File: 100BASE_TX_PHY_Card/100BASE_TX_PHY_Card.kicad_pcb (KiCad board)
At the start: 2 copper layers, 54 parts, among them J1 Conn_02x11_Odd_Even, J2 RJ45_Amphenol_RJMG1BD3B8K1ANR, SW1 SW_DIP_x07, U1 LAN8710A, Y1 25M

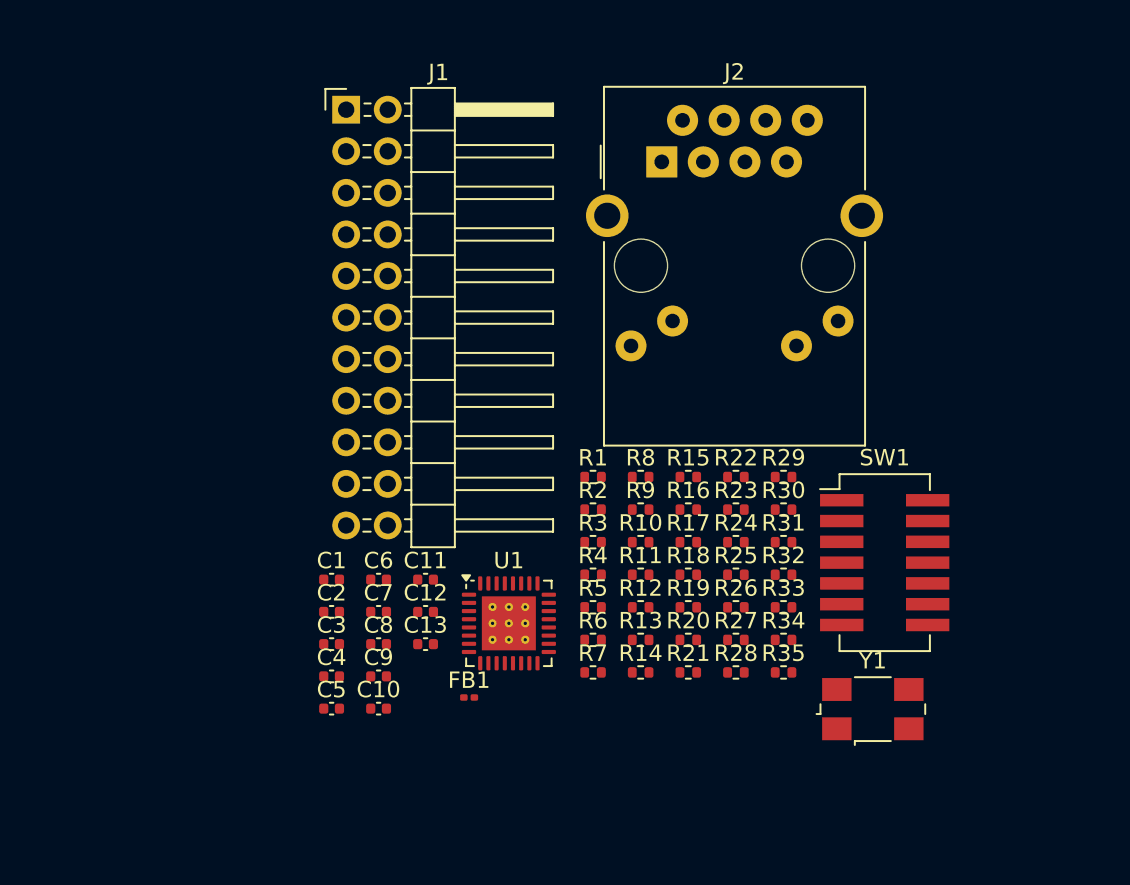
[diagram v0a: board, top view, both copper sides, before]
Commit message: LAN8710A PHY Card 4layer design
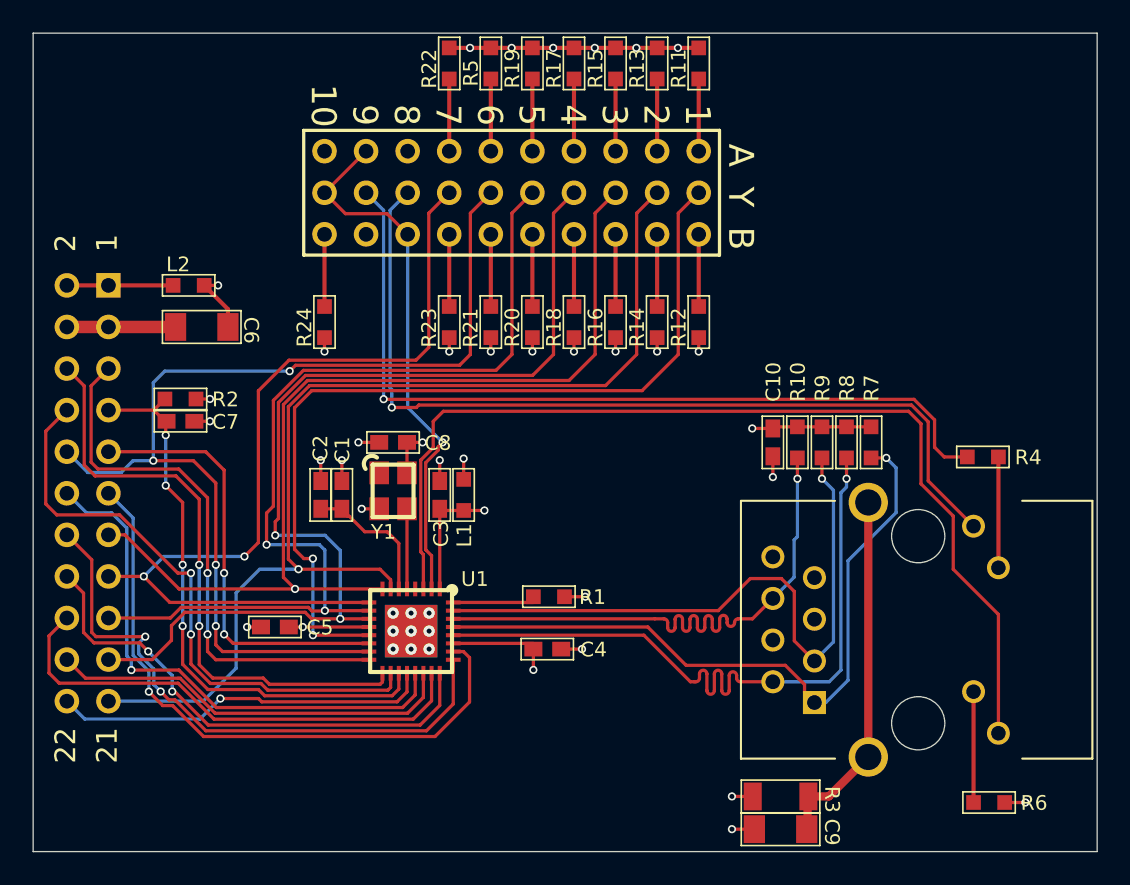
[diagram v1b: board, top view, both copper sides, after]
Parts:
- removed C11, C12, C13: dnp, Capacitor_SMD:C_0402_1005Metric
- removed FB1: FerriteBead, Resistor_SMD:R_0201_0603Metric
- removed J1: Conn_02x11_Odd_Even, Connector_PinHeader_2.54mm:PinHeader_2x11_P2.54mm_Horizontal
- removed J2: RJ45_Amphenol_RJMG1BD3B8K1ANR, Connector_RJ:RJ45_Amphenol_RJMG1BD3B8K1ANR
- removed R25, R26, R27, R28: 49,9, Resistor_SMD:R_0402_1005Metric
- removed R29: 0, Resistor_SMD:R_0402_1005Metric
- removed R30: 2,49k, Resistor_SMD:R_0402_1005Metric
- removed R31: 12.1k, Resistor_SMD:R_0402_1005Metric
- removed R32, R33: R, Resistor_SMD:R_0402_1005Metric
- removed R34, R35: 330, Resistor_SMD:R_0402_1005Metric
- removed SW1: SW_DIP_x07, Button_Switch_SMD:SW_DIP_SPSTx07_Slide_KingTek_DSHP07TJ_W5.25mm_P1.27mm_JPin
- added L1: Ferrite bead 120R/100MHz, pcSwitchLib.PcbLib:0603_IND, F.Cu at (142.3, 108.2)
- added L2: Ferrite bead 120R/100MHz, pcSwitchLib.PcbLib:0603_IND, F.Cu at (125.5, 95.4)
- added P1: RJMG1BD3B8K1ANR, pcSwitchLib.PcbLib:RJMG1BD3B8K1ANR, F.Cu at (170.1, 116.4)
- added P2: SELECTOR 10WAY, pcSwitchLib.PcbLib:SELECTOR_10WAY, F.Cu at (145.2, 89.8)
- added P3: Header 11X2H, Miscellaneous Connectors.IntLib:HDR2X11H, B.Cu at (120.6, 95.4)
- C1: value 30p -> 470pF 0603; footprint Capacitor_SMD:C_0402_1005Metric -> pcSwitchLib.PcbLib:0603_CAP
- C10: value dnp -> 15pF 0603; footprint Capacitor_SMD:C_0402_1005Metric -> pcSwitchLib.PcbLib:0603_CAP
- C2: value 30p -> 1uF 0603; footprint Capacitor_SMD:C_0402_1005Metric -> pcSwitchLib.PcbLib:0603_CAP
- C3, C4, C5: value 100n -> 100nF 0603; footprint Capacitor_SMD:C_0402_1005Metric -> pcSwitchLib.PcbLib:0603_CAP
- C6: value 4,7u -> 10uF 1206; footprint Capacitor_SMD:C_0402_1005Metric -> pcSwitchLib.PcbLib:1206_CAP
- C7: value 470p -> 100nF 0603; footprint Capacitor_SMD:C_0402_1005Metric -> pcSwitchLib.PcbLib:0603_CAP
- C8: value 1u -> 100nF 0603; footprint Capacitor_SMD:C_0402_1005Metric -> pcSwitchLib.PcbLib:0603_CAP
- C9: value dnp -> 10nF; footprint Capacitor_SMD:C_0402_1005Metric -> pcSwitchLib.PcbLib:1206_CAP
- R1: value 22 -> 12k1 0603; footprint Resistor_SMD:R_0402_1005Metric -> pcSwitchLib.PcbLib:0603
- R10, R9: value 1k -> 49R9 0603; footprint Resistor_SMD:R_0402_1005Metric -> pcSwitchLib.PcbLib:0603
- R11, R12, R13, R14, R15: value 1k -> 10k 0603; footprint Resistor_SMD:R_0402_1005Metric -> pcSwitchLib.PcbLib:0603
- R16, R17, R18, R19, R20, R21, R22: value 10k -> 10k 0603; footprint Resistor_SMD:R_0402_1005Metric -> pcSwitchLib.PcbLib:0603
- R2: value 22 -> 100k 0603; footprint Resistor_SMD:R_0402_1005Metric -> pcSwitchLib.PcbLib:0603
- R23: value 1M -> 10k 0603; footprint Resistor_SMD:R_0402_1005Metric -> pcSwitchLib.PcbLib:0603
- R24: value 2,49k -> 10k 0603; footprint Resistor_SMD:R_0402_1005Metric -> pcSwitchLib.PcbLib:0603
- R3: value 22 -> 1M 1206; footprint Resistor_SMD:R_0402_1005Metric -> pcSwitchLib.PcbLib:1206
- R4, R6: value 22 -> 330R 0603; footprint Resistor_SMD:R_0402_1005Metric -> pcSwitchLib.PcbLib:0603
- R5: value 22 -> 10k 0603; footprint Resistor_SMD:R_0402_1005Metric -> pcSwitchLib.PcbLib:0603
- R7, R8: value 22 -> 49R9 0603; footprint Resistor_SMD:R_0402_1005Metric -> pcSwitchLib.PcbLib:0603
- U1: footprint Package_DFN_QFN:QFN-32-1EP_5x5mm_P0.5mm_EP3.3x3.3mm_ThermalVias -> pcSwitchLib.PcbLib:LAN8710A
- Y1: value 25M -> 25MHz 3225; footprint Crystal:Crystal_SMD_0603-4Pin_6.0x3.5mm -> pcSwitchLib.PcbLib:XTAL_3225
- moved R13 35.2 mm to (154.1, 81.9), turned to -90 degrees
- moved R19 34.6 mm to (146.5, 81.9), turned to -90 degrees
- moved R5 33.8 mm to (144.0, 81.9), turned to -90 degrees
- moved Y1 32.2 mm to (138.0, 108.0), turned to -90 degrees
- moved R11 31.4 mm to (156.7, 81.9), turned to -90 degrees
- moved R22 30.7 mm to (141.4, 81.9), turned to -90 degrees
- moved R17 30.1 mm to (149.0, 81.9), turned to -90 degrees
- moved C10 29.1 mm to (161.2, 105.0), turned to 90 degrees
- moved R24 28.5 mm to (133.8, 97.7), turned to 90 degrees
- moved C9 26.3 mm to (161.7, 128.6)
- moved R6 26.2 mm to (174.4, 127.0)
- moved R2 26.1 mm to (125.0, 102.4)
- moved R15 25.7 mm to (151.6, 81.9), turned to -90 degrees
- moved R4 24.9 mm to (174.0, 105.9), turned to 180 degrees
- moved R21 24.6 mm to (144.0, 97.7), turned to 90 degrees
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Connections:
- C1 pad 1: Net-(U1-XTAL2) -> GND
- C1 pad 2: GND -> VDDCR
- C10 pad 1: /TX_N -> GND
- C10 pad 2: GND -> VDD_A
- C2 pad 1: Net-(U1-XTAL1/CLKIN) -> GND
- C2 pad 2: GND -> VDDCR
- C3 pad 2: +3V3 -> VDD_A
- C4 pad 2: AVDD -> VDD_A
- C5 pad 2: AVDD -> VDDIO
- C6 pad 2: AVDD -> VDDIO
- C7 pad 2: /VDDCR -> PHY_RST
- C8 pad 2: /VDDCR -> VDDIO
- C9 pad 1: /TX_P -> GND
- C9 pad 2: GND -> SHIELD
- R1 pad 1: RXD0 -> NetR1_1
- R1 pad 2: /RXD0/~{MODE0} -> GND
- R10 pad 1: Net-(R10-Pad1) -> VDD_A
- R10 pad 2: +3V3 -> RX_n
- R11 pad 1: Net-(R11-Pad1) -> VCC_3V3
- R11 pad 2: +3V3 -> NetP2_1
- R12 pad 1: Net-(R12-Pad1) -> GND
- R12 pad 2: +3V3 -> NetP2_3
- R13 pad 1: Net-(R13-Pad1) -> VCC_3V3
- R13 pad 2: +3V3 -> NetP2_4
- R14 pad 1: Net-(R14-Pad1) -> GND
- R14 pad 2: +3V3 -> NetP2_6
- R15 pad 1: Net-(R15-Pad1) -> VCC_3V3
- R15 pad 2: +3V3 -> NetP2_7
- R16 pad 1: /RXD0/~{MODE0} -> GND
- R16 pad 2: GND -> NetP2_9
- R17 pad 1: /COL/~{MODE2} -> VCC_3V3
- R17 pad 2: GND -> NetP2_10
- R18 pad 1: /RXER/~{PHYAD0} -> GND
- R18 pad 2: GND -> NetP2_12
- R19 pad 1: /RXD3/~{PHYAD2} -> VCC_3V3
- R19 pad 2: GND -> NetP2_13
- R2 pad 1: RXD1 -> PHY_RST
- R2 pad 2: /RXD1/~{MODE1} -> VCC_3V3
- R20 pad 1: /RXD1/~{MODE1} -> GND
- R20 pad 2: GND -> NetP2_15
- R21 pad 1: /RXD2/~{RMIISEL} -> GND
- R21 pad 2: GND -> NetP2_18
- R22 pad 1: /RXCLK/~{PHYAD1} -> VCC_3V3
- R22 pad 2: GND -> NetP2_19
- R23 pad 1: Net-(U1-XTAL1/CLKIN) -> GND
- R23 pad 2: Net-(U1-XTAL2) -> NetP2_21
- R24 pad 1: +3V3 -> GND
- R24 pad 2: ~{PHY_RESET} -> NetP2_30
- R3 pad 1: RXD2 -> SHIELD
- R3 pad 2: /RXD2/~{RMIISEL} -> GND
- R4 pad 1: RXD3 -> NetP1_L2
- R4 pad 2: /RXD3/~{PHYAD2} -> LED2-
- R5 pad 1: RXDV -> VCC_3V3
- R5 pad 2: Net-(U1-RXDV) -> NetP2_16
- R6 pad 1: RXCLK -> NetP1_L3
- R6 pad 2: /RXCLK/~{PHYAD1} -> GND
- R7 pad 1: COL -> VDD_A
- R7 pad 2: /COL/~{MODE2} -> TX_p
- R8 pad 1: CRS -> VDD_A
- R8 pad 2: /R_CRS -> TX_n
- R9 pad 1: Net-(R9-Pad1) -> VDD_A
- R9 pad 2: +3V3 -> RX_p
- U1 pad 1: AVDD -> VDD_A
- U1 pad 10: /RXD1/~{MODE1} -> /MODE1
- U1 pad 11: /RXD0/~{MODE0} -> /MODE0
- U1 pad 12: +3V3 -> VDDIO
- U1 pad 13: /RXER/~{PHYAD0} -> /PHYAD0
- U1 pad 14: /R_CRS -> CRS
- U1 pad 15: /COL/~{MODE2} -> /MODE2
- U1 pad 18: Net-(U1-~{INT}/TXER/TXD4) -> PHY_IRQ
- U1 pad 19: ~{PHY_RESET} -> PHY_RST
- U1 pad 26: Net-(U1-RXDV) -> RXDV
- U1 pad 27: AVDD -> VDD_A
- U1 pad 28: /TX_N -> TX_n
- U1 pad 29: /TX_P -> TX_p
- U1 pad 30: /RX_N -> RX_n
- U1 pad 31: /RX_P -> RX_p
- U1 pad 32: Net-(U1-RBIAS) -> NetR1_1
- U1 pad 4: Net-(U1-XTAL2) -> (no net)
- U1 pad 5: Net-(U1-XTAL1/CLKIN) -> NetU1_5
- U1 pad 6: /VDDCR -> VDDCR
- U1 pad 7: /RXCLK/~{PHYAD1} -> /PHYAD1
- U1 pad 8: /RXD3/~{PHYAD2} -> /PHYAD2
- U1 pad 9: /RXD2/~{RMIISEL} -> /RMIISEL
- Y1 pad 1: Net-(U1-XTAL2) -> (no net)
- Y1 pad 2: Net-(U1-XTAL1/CLKIN) -> GND
- Y1 pad 3: (no net) -> NetU1_5
- Y1 pad 4: (no net) -> VDDIO
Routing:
- net VDD_A: track 0.00 -> 90.4 mm, vias 0 -> 3
- net /PHYAD1: track 0.00 -> 67.3 mm, vias 0 -> 1
- net /MODE2: track 0.00 -> 65.1 mm, vias 0 -> 4
- net /MODE0: track 0.00 -> 62.9 mm, vias 0 -> 2
- net LED1: track 0.00 -> 61.9 mm
- net /PHYAD2: track 0.00 -> 60.4 mm, vias 0 -> 1
- net /MODE1: track 0.00 -> 58.8 mm, vias 0 -> 2
- net /RMIISEL: track 0.00 -> 55.2 mm, vias 0 -> 2
- net LED2+: track 0.00 -> 54.4 mm, vias 0 -> 1
- net /PHYAD0: track 0.00 -> 53.3 mm, vias 0 -> 2
- net LED2-: track 0.00 -> 51.1 mm, vias 0 -> 1
- net VDDIO: track 0.00 -> 50.1 mm, vias 0 -> 3
- net TX_n: track 0.00 -> 43.8 mm, vias 0 -> 1
- net TX_p: track 0.00 -> 43.2 mm, vias 0 -> 1
- net RX_p: track 0.00 -> 39.9 mm, vias 0 -> 1
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- added copper zone on In1.Cu, net GND
- added copper zone on In2.Cu, net VCC_3V3
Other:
- board outline added: 65 x 50 mm
- copper layers 2 -> 4
- rule pad_to_mask_clearance: 0 -> 0.075
